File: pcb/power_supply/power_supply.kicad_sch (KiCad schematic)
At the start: 25 parts, among them J1 LINE, J5 EARTH, SW1 SW_DPDT_x2, U1 AP63203WU

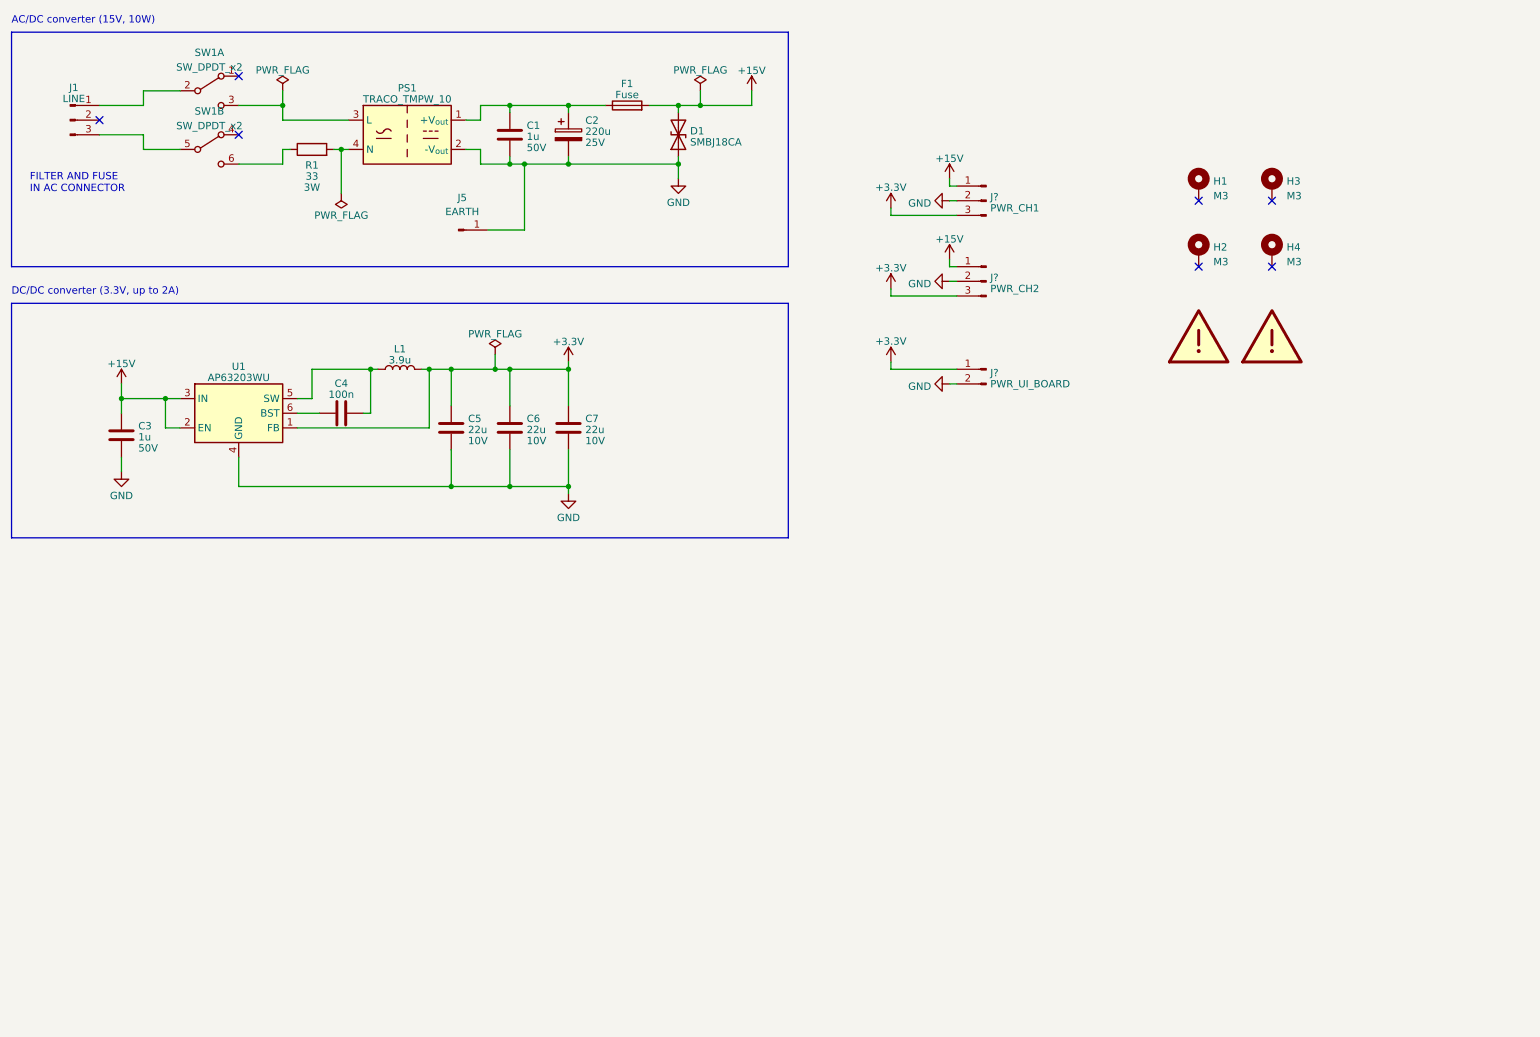
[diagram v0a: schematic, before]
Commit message: Update power supply  KiCAD project to v8 and fix incorrect R1 resistor value
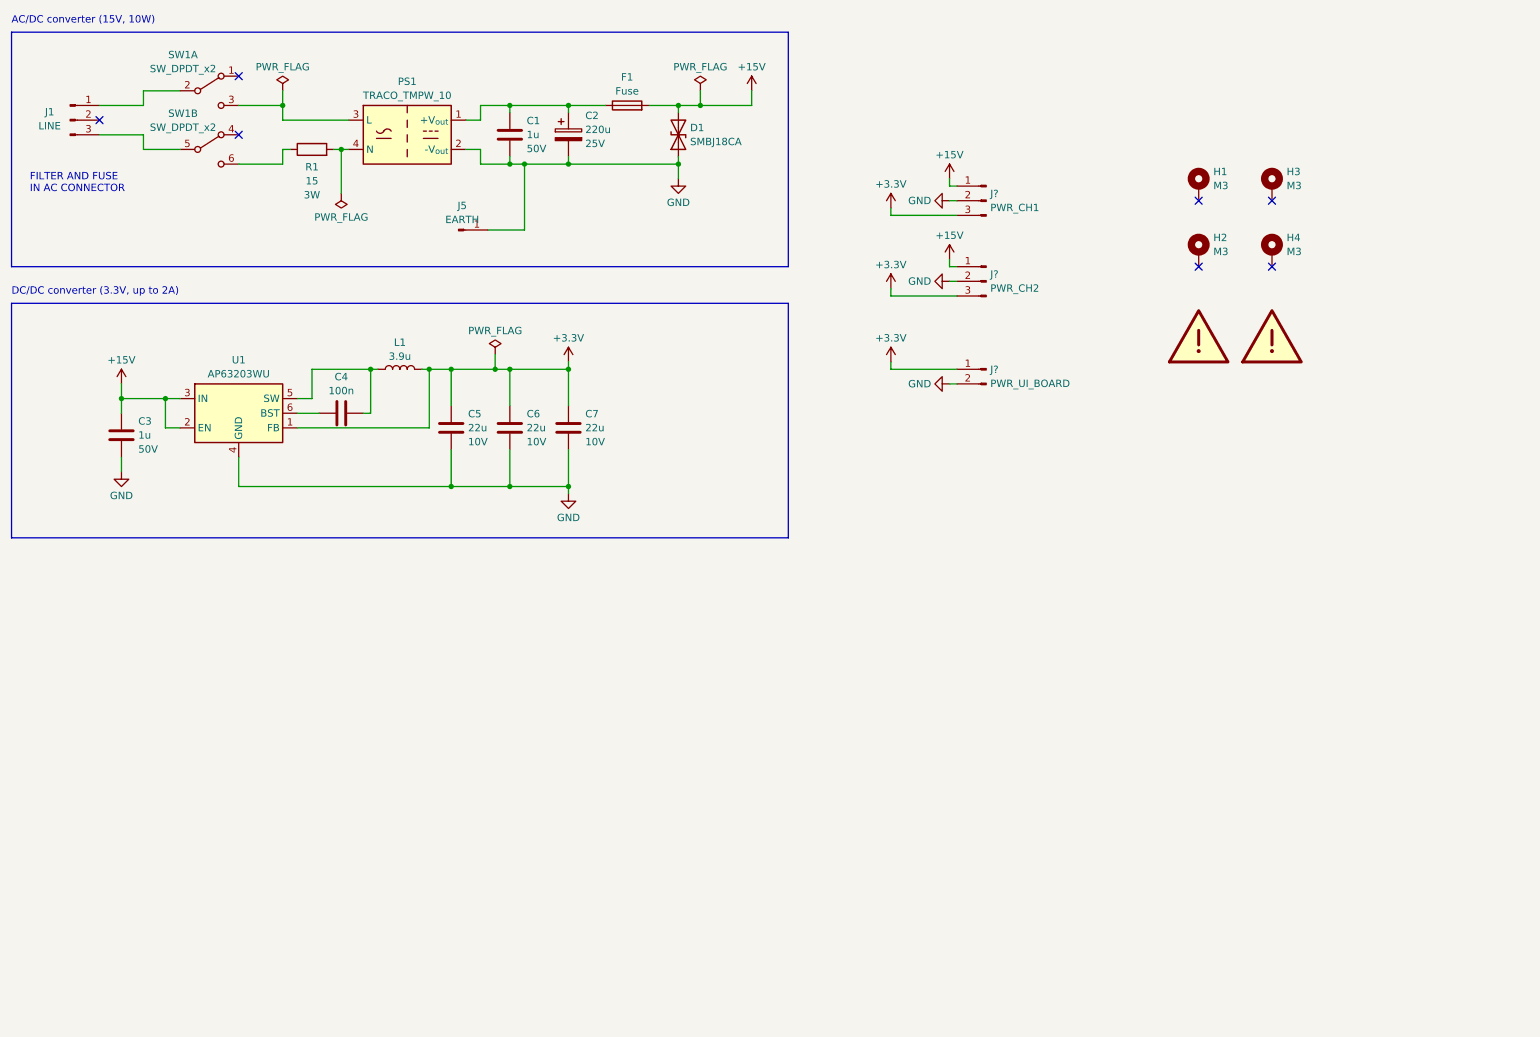
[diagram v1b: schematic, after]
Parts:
- R1: value 33 -> 15

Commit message: Update to Kicad v9, new power supply board and other modifications
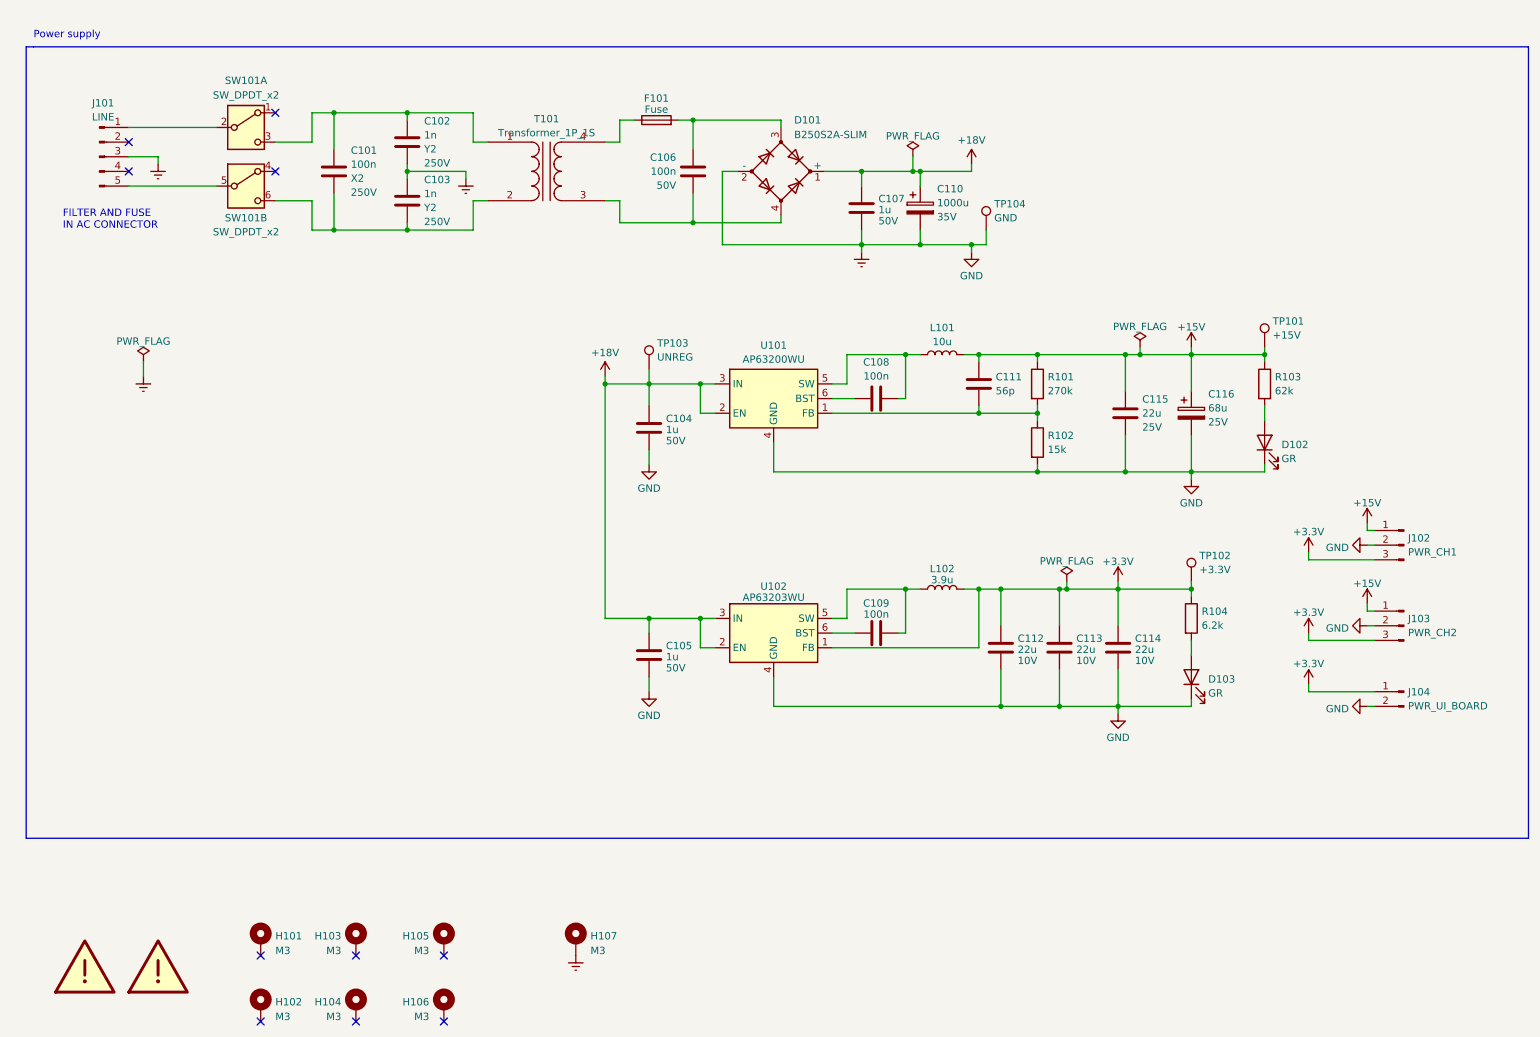
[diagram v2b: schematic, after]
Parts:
- removed D1: SMBJ18CA, Diode_SMD:D_SMB, symbol Device:D_TVS
- removed J5: EARTH, 01_Sebastian:BananaJack_Connector, symbol Connector:Conn_01x01_Pin
- removed PS1: TRACO_TMPW_10, 01_Sebastian:TRACO_TMPW_10, symbol 01_Sebastian:TRACO_TMPW_10
- removed R1: 15, Resistor_THT:R_Axial_DIN0617_L17.0mm_D6.0mm_P20.32mm_Horizontal, symbol Device:R
- added C101: 100n, Capacitor_THT:C_Rect_L18.0mm_W5.0mm_P15.00mm_FKS3_FKP3, symbol Device:C
- added C102, C103: 1n, Capacitor_THT:C_Rect_L13.5mm_W5.0mm_P10.00mm_FKS3_FKP3_MKS4, symbol Device:C
- added C104: 1u, Capacitor_SMD:C_1206_3216Metric, symbol Device:C
- added C106: 100n, Capacitor_SMD:C_0805_2012Metric, symbol Device:C
- added C108: 100n, Capacitor_SMD:C_0603_1608Metric, symbol Device:C
- added C111: 56p, Capacitor_SMD:C_0603_1608Metric, symbol Device:C
- added C115: 22u, Capacitor_SMD:C_1206_3216Metric, symbol Device:C
- added C116: 68u, Capacitor_SMD:C_Elec_6.3x5.8, symbol Device:C_Polarized
- added D101: B250S2A-SLIM, Diode_SMD:Diode_Bridge_Diotec_SO-DIL-Slim, symbol Device:D_Bridge_+-AA
- added D102, D103: GR, LED_SMD:LED_0603_1608Metric, symbol Device:LED
- added H105, H106: M3, MountingHole:MountingHole_3.2mm_M3_DIN965_Pad, symbol Mechanical:MountingHole_Pad
- added H107: M3, MountingHole:MountingHole_2.2mm_M2_DIN965_Pad, symbol Mechanical:MountingHole_Pad
- added L101: 10u, Inductor_SMD:L_Bourns-SRN4018, symbol Device:L
- added R101: 270k, Resistor_SMD:R_0603_1608Metric, symbol Device:R
- added R102: 15k, Resistor_SMD:R_0603_1608Metric, symbol Device:R
- added R103: 62k, Resistor_SMD:R_0603_1608Metric, symbol Device:R
- added R104: 6.2k, Resistor_SMD:R_0603_1608Metric, symbol Device:R
- added T101: Transformer_1P_1S, 01_Sebastian:BLOCK_VC16_1, symbol Device:Transformer_1P_1S
- added TP101: +15V, TestPoint:TestPoint_Keystone_5000-5004_Miniature, symbol Connector:TestPoint
- added TP102: +3.3V, TestPoint:TestPoint_Keystone_5000-5004_Miniature, symbol Connector:TestPoint
- added TP103: UNREG, TestPoint:TestPoint_Keystone_5000-5004_Miniature, symbol Connector:TestPoint
- added TP104: GND, TestPoint:TestPoint_Keystone_5000-5004_Miniature, symbol Connector:TestPoint
- added U101: AP63200WU, Package_TO_SOT_SMD:TSOT-23-6, symbol Regulator_Switching:AP63203WU
- C105: renamed from C3; footprint 01_Sebastian:C_0805_2012Metric_Box -> Capacitor_SMD:C_1206_3216Metric
- C107: renamed from C1; footprint 01_Sebastian:C_0805_2012Metric_Box -> Capacitor_SMD:C_0805_2012Metric
- C109: renamed from C4; footprint 01_Sebastian:C_0805_2012Metric_Box -> Capacitor_SMD:C_0603_1608Metric
- C110: renamed from C2; value 220u -> 1000u; footprint Capacitor_THT:CP_Radial_D8.0mm_P5.00mm -> Capacitor_THT:CP_Radial_D16.0mm_P7.50mm; Voltage Rating 25V -> 35V
- C112: renamed from C5; footprint 01_Sebastian:C_1206_3216Metric_Box -> Capacitor_SMD:C_1206_3216Metric
- C113: renamed from C6; footprint 01_Sebastian:C_1206_3216Metric_Box -> Capacitor_SMD:C_1206_3216Metric
- C114: renamed from C7; footprint 01_Sebastian:C_1206_3216Metric_Box -> Capacitor_SMD:C_1206_3216Metric
- F101: renamed from F1; footprint Fuse:Fuse_0805_2012Metric -> Fuse:Fuse_1206_3216Metric
- J101: renamed from J1; footprint Connector_Molex:Molex_KK-396_A-41791-0003_1x03_P3.96mm_Vertical -> Connector_Molex:Molex_KK-396_A-41791-0005_1x05_P3.96mm_Vertical; symbol Connector:Conn_01x03_Pin -> Connector:Conn_01x05_Pin
- L102: renamed from L1; footprint Inductor_SMD:L_Bourns-SRN6028 -> Inductor_SMD:L_Bourns-SRN4018
- gave numbers to parts that had none: 3
- renumbered H1 to H101, H2 to H102, H3 to H103, H4 to H104, LOGO1 to LOGO101, LOGO2 to LOGO102, SW1 to SW101, U1 to U102
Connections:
- net +15V: now also C111.2, C115.1, C116.1, L101.2, R101.1, R103.1, TP101.1; no longer C105.1, F101.2, U102.2 (EN), U102.3 (IN)
- net +3.3V: now also R104.1, TP102.1
- net at SW101.5 (B): now also J101.5 (Pin_5); no longer J101.3 (Pin_3)
- net at SW101.6 (C): now also C101.2, C103.2, T101.2 (AB)
- net +18V: now reaches C107.1, C110.1
- net +18V: now also C105.1, U102.2 (EN), U102.3 (IN), C104.1, D101.1 (+), TP103.1, U101.2 (EN), U101.3 (IN); no longer F101.1
- net at SW101.3 (C): now also C101.1, C102.1, T101.1 (AA)
- net GND renamed Earth
- net Earth: now also J101.3 (Pin_3), C102.2, C103.1, C104.2, C115.2, C116.2, D101.2 (-), D102.1 (K), D103.1 (K), H107.1, R102.2, TP104.1, U101.4 (GND)
- new net: C106.1, D101.3, F101.2
- new net: C106.2, D101.4, T101.3 (SA)
- new net: C111.1, R101.2, R102.1, U101.1 (FB)
- new net: D103.2 (A), R104.2
- new net: C108.2, L101.1, U101.5 (SW)
- new net: C108.1, U101.6 (BST)
- new net: D102.2 (A), R103.2
- new net: F101.1, T101.4 (SB)
- no-connect marks 7 -> 10
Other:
- note added: "Power supply"
- note removed: "AC/DC converter (15V, 10W)"
- note removed: "DC/DC converter (3.3V, up to 2A)"
- company: Sebastian Harnisch -> (none)
- title: Power Supply for Programmable Precision Resistor -> (none)
- moved on the sheet: C105, C107, C109, C110, C112, C113, C114, F101, H101, H102, H103, H104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
